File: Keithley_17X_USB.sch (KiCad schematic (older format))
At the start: 42 parts, among them J1 USB_B, J2 SIGNAL INPUT, J3 PROG, U1 TLP281-4, U2 TLP281-4, U3 MIC5504-3.3YM5, U4 MSP430FR2110, U5 FT230XS

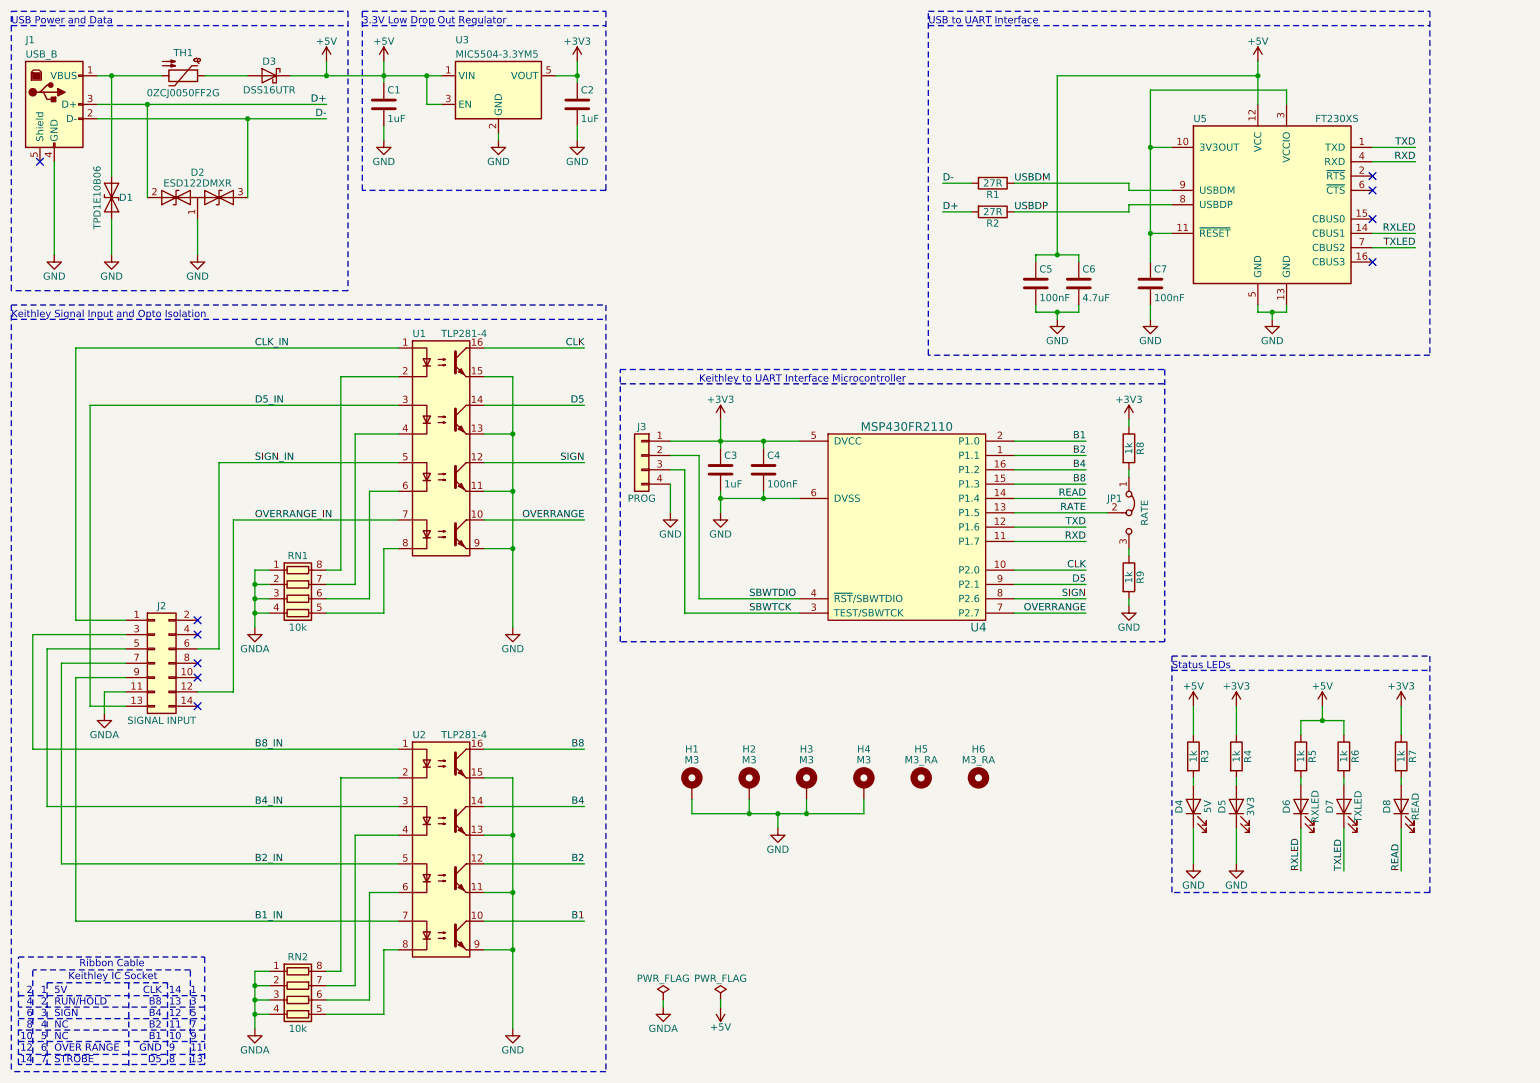
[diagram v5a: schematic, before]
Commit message: connect usb sheild to ground
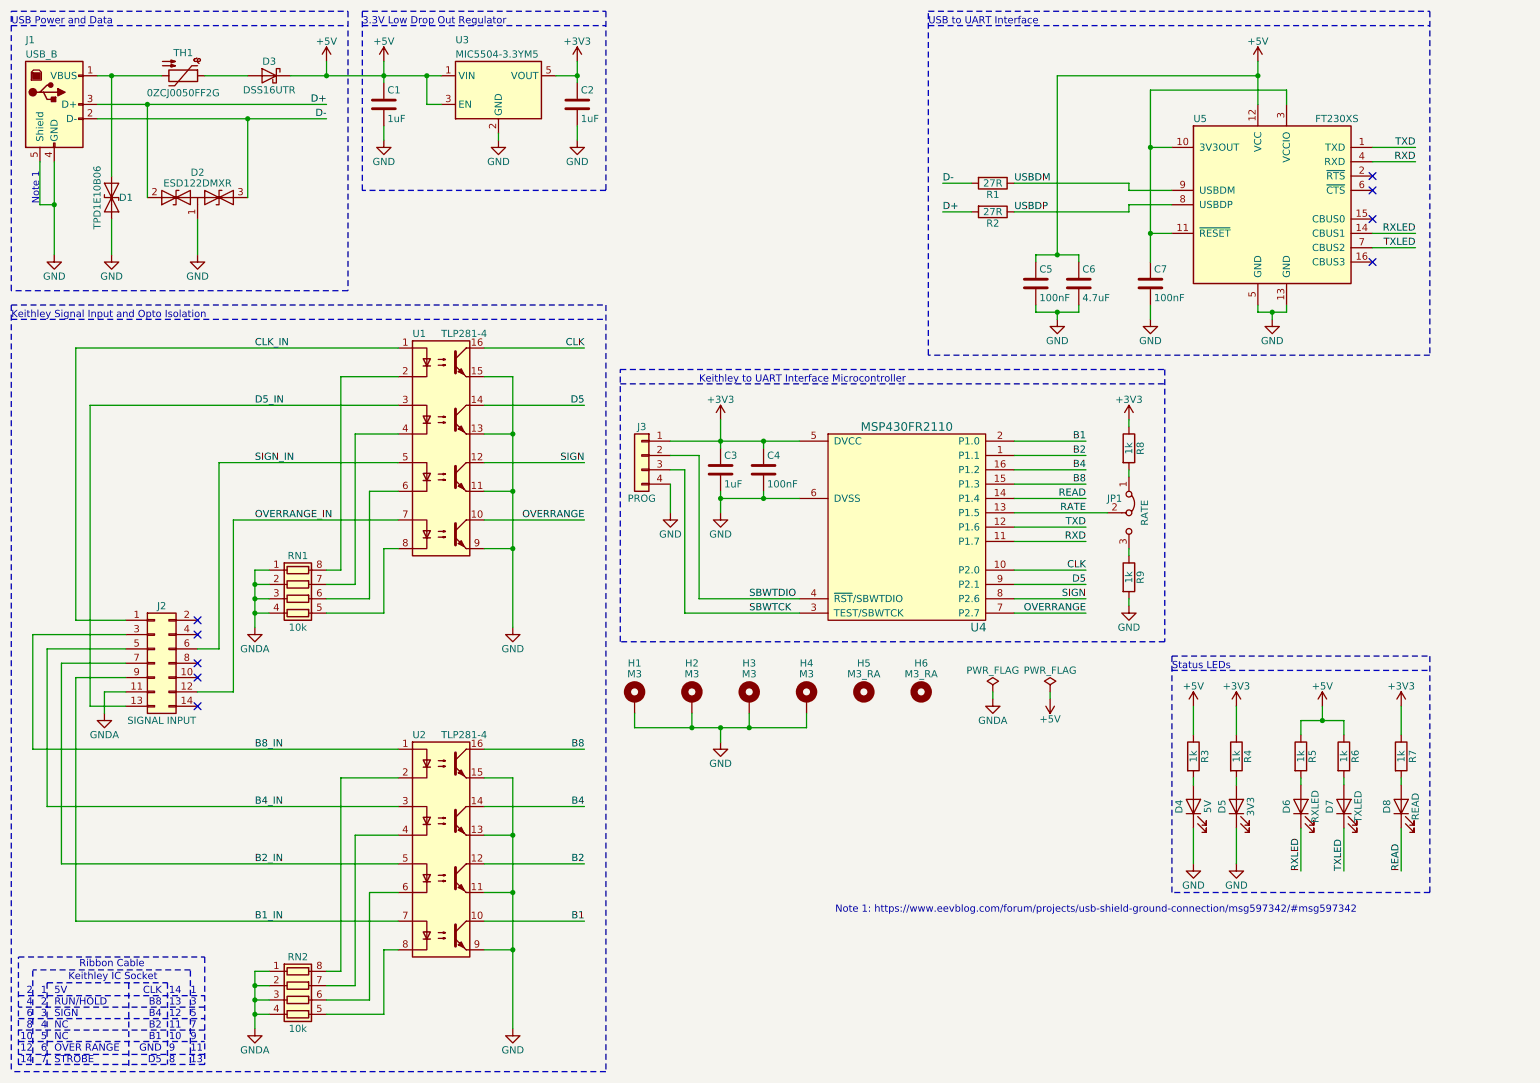
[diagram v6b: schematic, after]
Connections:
- net GND: now also J1.5 (Shield)
- no-connect marks 10 -> 9
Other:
- note added: "Note 1"
- note added: "Note 1: https://www.eevblog.com/forum/projects/usb-shield-ground-connection/msg597342/#msg597342"
- moved on the sheet: H1, H2, H3, H4, H5, H6
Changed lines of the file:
@@
 	1    0    0    -1
 $EndComp
-NoConn ~ 750  1600
 $Comp
 L power:GND #PWR026
@@
 $EndComp
 Wire Wire Line
-	850  1600 850  2250
+	850  1600 850  1900
 $Comp
 L power:GND #PWR03
@@
 L Mechanical:MountingHole_Pad H1
 U 1 1 5C68020E
-P 5300 5950
-F 0 "H1" H 5300 6200 50  0000 C CNN
-F 1 "M3" H 5300 6125 50  0000 C CNN
-F 2 "MountingHole:MountingHole_3.2mm_M3_DIN965_Pad" H 5300 5950 50  0001 C CNN
-F 3 "~" H 5300 5950 50  0001 C CNN
-	1    5300 5950
+P 4900 5350
+F 0 "H1" H 4900 5600 50  0000 C CNN
+F 1 "M3" H 4900 5525 50  0000 C CNN
+F 2 "MountingHole:MountingHole_3.2mm_M3_DIN965_Pad" H 4900 5350 50  0001 C CNN
+F 3 "~" H 4900 5350 50  0001 C CNN
+	1    4900 5350
 	1    0    0    -1
 $EndComp
@@
 L power:GND #PWR018
 U 1 1 5C680CDB
-P 5900 6250
-F 0 "#PWR018" H 5900 6000 50  0001 C CNN
-F 1 "GND" H 5900 6100 50  0000 C CNN
-F 2 "" H 5900 6250 50  0001 C CNN
-F 3 "" H 5900 6250 50  0001 C CNN
-	1    5900 6250
-	1    0    0    -1
-$EndComp
-Wire Wire Line
-	5300 6050 5300 6150
-Wire Wire Line
-	5300 6150 5700 6150
-Wire Wire Line
-	6500 6150 6500 6050
-Wire Wire Line
-	6100 6050 6100 6150
-Connection ~ 6100 6150
-Wire Wire Line
-	6100 6150 6500 6150
-Wire Wire Line
-	5700 6050 5700 6150
-Connection ~ 5700 6150
-Wire Wire Line
-	5700 6150 5900 6150
-Wire Wire Line
-	5900 6250 5900 6150
-Connection ~ 5900 6150
-Wire Wire Line
-	5900 6150 6100 6150
+P 5500 5650
+F 0 "#PWR018" H 5500 5400 50  0001 C CNN
+F 1 "GND" H 5500 5500 50  0000 C CNN
+F 2 "" H 5500 5650 50  0001 C CNN
+F 3 "" H 5500 5650 50  0001 C CNN
+	1    5500 5650
+	1    0    0    -1
+$EndComp
+Wire Wire Line
+	4900 5450 4900 5550
+Wire Wire Line
+	4900 5550 5300 5550
+Wire Wire Line
+	6100 5550 6100 5450
+Wire Wire Line
+	5700 5450 5700 5550
+Connection ~ 5700 5550
+Wire Wire Line
+	5700 5550 6100 5550
+Wire Wire Line
+	5300 5450 5300 5550
+Connection ~ 5300 5550
+Wire Wire Line
+	5300 5550 5500 5550
+Wire Wire Line
+	5500 5650 5500 5550
+Connection ~ 5500 5550
+Wire Wire Line
+	5500 5550 5700 5550
 $Comp
 L Mechanical:MountingHole_Pad H2
 U 1 1 5C6B7AB1
-P 5700 5950
-F 0 "H2" H 5700 6200 50  0000 C CNN
-F 1 "M3" H 5700 6125 50  0000 C CNN
-F 2 "MountingHole:MountingHole_3.2mm_M3_DIN965_Pad" H 5700 5950 50  0001 C CNN
-F 3 "~" H 5700 5950 50  0001 C CNN
-	1    5700 5950
+P 5300 5350
+F 0 "H2" H 5300 5600 50  0000 C CNN
+F 1 "M3" H 5300 5525 50  0000 C CNN
+F 2 "MountingHole:MountingHole_3.2mm_M3_DIN965_Pad" H 5300 5350 50  0001 C CNN
+F 3 "~" H 5300 5350 50  0001 C CNN
+	1    5300 5350
 	1    0    0    -1
 $EndComp
@@
 L Mechanical:MountingHole_Pad H3
 U 1 1 5C6B7B0F
-P 6100 5950
-F 0 "H3" H 6100 6200 50  0000 C CNN
-F 1 "M3" H 6100 6125 50  0000 C CNN
-F 2 "MountingHole:MountingHole_3.2mm_M3_DIN965_Pad" H 6100 5950 50  0001 C CNN
-F 3 "~" H 6100 5950 50  0001 C CNN
-	1    6100 5950
+P 5700 5350
+F 0 "H3" H 5700 5600 50  0000 C CNN
+F 1 "M3" H 5700 5525 50  0000 C CNN
+F 2 "MountingHole:MountingHole_3.2mm_M3_DIN965_Pad" H 5700 5350 50  0001 C CNN
+F 3 "~" H 5700 5350 50  0001 C CNN
+	1    5700 5350
 	1    0    0    -1
 $EndComp
@@
 L Mechanical:MountingHole_Pad H4
 U 1 1 5C6B7B6B
-P 6500 5950
-F 0 "H4" H 6500 6200 50  0000 C CNN
-F 1 "M3" H 6500 6125 50  0000 C CNN
-F 2 "MountingHole:MountingHole_3.2mm_M3_DIN965_Pad" H 6500 5950 50  0001 C CNN
-F 3 "~" H 6500 5950 50  0001 C CNN
-	1    6500 5950
+P 6100 5350
+F 0 "H4" H 6100 5600 50  0000 C CNN
+F 1 "M3" H 6100 5525 50  0000 C CNN
+F 2 "MountingHole:MountingHole_3.2mm_M3_DIN965_Pad" H 6100 5350 50  0001 C CNN
+F 3 "~" H 6100 5350 50  0001 C CNN
+	1    6100 5350
 	1    0    0    -1
 $EndComp
@@
 L power:PWR_FLAG #FLG0101
 U 1 1 5C804C0D
-P 5100 7450
-F 0 "#FLG0101" H 5100 7525 50  0001 C CNN
-F 1 "PWR_FLAG" H 5100 7600 50  0000 C CNN
-F 2 "" H 5100 7450 50  0001 C CNN
-F 3 "~" H 5100 7450 50  0001 C CNN
-	1    5100 7450
+P 7400 5300
+F 0 "#FLG0101" H 7400 5375 50  0001 C CNN
+F 1 "PWR_FLAG" H 7400 5450 50  0000 C CNN
+F 2 "" H 7400 5300 50  0001 C CNN
+F 3 "~" H 7400 5300 50  0001 C CNN
+	1    7400 5300
 	1    0    0    -1
 $EndComp
@@
 L power:GNDA #PWR0101
 U 1 1 5C804D47
-P 5100 7500
-F 0 "#PWR0101" H 5100 7250 50  0001 C CNN
-F 1 "GNDA" H 5100 7350 50  0000 C CNN
-F 2 "" H 5100 7500 50  0001 C CNN
-F 3 "" H 5100 7500 50  0001 C CNN
-	1    5100 7500
-	1    0    0    -1
-$EndComp
-Wire Wire Line
-	5100 7500 5100 7450
+P 7400 5350
+F 0 "#PWR0101" H 7400 5100 50  0001 C CNN
+F 1 "GNDA" H 7400 5200 50  0000 C CNN
+F 2 "" H 7400 5350 50  0001 C CNN
+F 3 "" H 7400 5350 50  0001 C CNN
+	1    7400 5350
+	1    0    0    -1
+$EndComp
+Wire Wire Line
+	7400 5350 7400 5300
 $Comp
 L power:+5V #PWR0102
 U 1 1 5C830718
-P 5500 7500
-F 0 "#PWR0102" H 5500 7350 50  0001 C CNN
-F 1 "+5V" H 5500 7640 50  0000 C CNN
-F 2 "" H 5500 7500 50  0001 C CNN
-F 3 "" H 5500 7500 50  0001 C CNN
-	1    5500 7500
+P 7800 5350
+F 0 "#PWR0102" H 7800 5200 50  0001 C CNN
+F 1 "+5V" H 7800 5490 50  0000 C CNN
+F 2 "" H 7800 5350 50  0001 C CNN
+F 3 "" H 7800 5350 50  0001 C CNN
+	1    7800 5350
 	-1   0    0    1
 $EndComp
@@
 L power:PWR_FLAG #FLG0102
 U 1 1 5C84C9A6
-P 5500 7450
-F 0 "#FLG0102" H 5500 7525 50  0001 C CNN
-F 1 "PWR_FLAG" H 5500 7600 50  0000 C CNN
-F 2 "" H 5500 7450 50  0001 C CNN
-F 3 "~" H 5500 7450 50  0001 C CNN
-	1    5500 7450
-	1    0    0    -1
-$EndComp
-Wire Wire Line
-	5500 7450 5500 7500
+P 7800 5300
+F 0 "#FLG0102" H 7800 5375 50  0001 C CNN
+F 1 "PWR_FLAG" H 7800 5450 50  0000 C CNN
+F 2 "" H 7800 5300 50  0001 C CNN
+F 3 "~" H 7800 5300 50  0001 C CNN
+	1    7800 5300
+	1    0    0    -1
+$EndComp
+Wire Wire Line
+	7800 5300 7800 5350
 $Comp
 L Mechanical:MountingHole H5
 U 1 1 5C6C1140
-P 6900 5900
-F 0 "H5" H 6900 6100 50  0000 C CNN
-F 1 "M3_RA" H 6900 6025 50  0000 C CNN
-F 2 "Terminal_Keystone:Keystone_Screw-Terminal_7761_RightAngle" H 6900 5900 50  0001 C CNN
-F 3 "http://www.keyelco.com/product-pdf.cfm?p=3928" H 6900 5900 50  0001 C CNN
-F 4 "TERM SCREW M3 4 PIN PCB RA" H 6900 5900 50  0001 C CNN "Description"
-F 5 "Keystone Electronics" H 6900 5900 50  0001 C CNN "Manufacture"
-F 6 "7761" H 6900 5900 50  0001 C CNN "Mfg Part Number"
-F 7 "Digi-Key" H 6900 5900 50  0001 C CNN "Supplier"
-F 8 "36-7761-ND" H 6900 5900 50  0001 C CNN "Supplier Part Number"
-	1    6900 5900
+P 6500 5300
+F 0 "H5" H 6500 5500 50  0000 C CNN
+F 1 "M3_RA" H 6500 5425 50  0000 C CNN
+F 2 "Terminal_Keystone:Keystone_Screw-Terminal_7761_RightAngle" H 6500 5300 50  0001 C CNN
+F 3 "http://www.keyelco.com/product-pdf.cfm?p=3928" H 6500 5300 50  0001 C CNN
+F 4 "TERM SCREW M3 4 PIN PCB RA" H 6500 5300 50  0001 C CNN "Description"
+F 5 "Keystone Electronics" H 6500 5300 50  0001 C CNN "Manufacture"
+F 6 "7761" H 6500 5300 50  0001 C CNN "Mfg Part Number"
+F 7 "Digi-Key" H 6500 5300 50  0001 C CNN "Supplier"
+F 8 "36-7761-ND" H 6500 5300 50  0001 C CNN "Supplier Part Number"
+	1    6500 5300
 	1    0    0    -1
 $EndComp
@@
 L Mechanical:MountingHole H6
 U 1 1 5C6C2A25
-P 7300 5900
-F 0 "H6" H 7300 6100 50  0000 C CNN
-F 1 "M3_RA" H 7300 6025 50  0000 C CNN
-F 2 "Terminal_Keystone:Keystone_Screw-Terminal_7761_RightAngle" H 7300 5900 50  0001 C CNN
-F 3 "http://www.keyelco.com/product-pdf.cfm?p=3928" H 7300 5900 50  0001 C CNN
-F 4 "TERM SCREW M3 4 PIN PCB RA" H 7300 5900 50  0001 C CNN "Description"
-F 5 "Keystone Electronics" H 7300 5900 50  0001 C CNN "Manufacture"
-F 6 "7761" H 7300 5900 50  0001 C CNN "Mfg Part Number"
-F 7 "Digi-Key" H 7300 5900 50  0001 C CNN "Supplier"
-F 8 "36-7761-ND" H 7300 5900 50  0001 C CNN "Supplier Part Number"
-	1    7300 5900
+P 6900 5300
+F 0 "H6" H 6900 5500 50  0000 C CNN
+F 1 "M3_RA" H 6900 5425 50  0000 C CNN
+F 2 "Terminal_Keystone:Keystone_Screw-Terminal_7761_RightAngle" H 6900 5300 50  0001 C CNN
+F 3 "http://www.keyelco.com/product-pdf.cfm?p=3928" H 6900 5300 50  0001 C CNN
+F 4 "TERM SCREW M3 4 PIN PCB RA" H 6900 5300 50  0001 C CNN "Description"
+F 5 "Keystone Electronics" H 6900 5300 50  0001 C CNN "Manufacture"
+F 6 "7761" H 6900 5300 50  0001 C CNN "Mfg Part Number"
+F 7 "Digi-Key" H 6900 5300 50  0001 C CNN "Supplier"
+F 8 "36-7761-ND" H 6900 5300 50  0001 C CNN "Supplier Part Number"
+	1    6900 5300
 	1    0    0    -1
 $EndComp
@@
 Text Label 7550 1950 0    50   ~ 0
 USBDP
+Wire Wire Line
+	750  1600 750  1900
+Wire Wire Line
+	750  1900 850  1900
+Connection ~ 850  1900
+Wire Wire Line
+	850  1900 850  2250
+Text Notes 750  1900 1    50   ~ 0
+Note 1
+Text Notes 6300 6850 0    50   ~ 0
+Note 1: https://www.eevblog.com/forum/projects/usb-shield-ground-connection/msg597342/#msg597342
 $EndSCHEMATC

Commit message: ground right angle mounts
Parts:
- H5, H6: symbol Mechanical:MountingHole -> Mechanical:MountingHole_Pad
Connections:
- net GND: now also H5.1, H6.1
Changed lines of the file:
@@
 	7800 5300 7800 5350
 $Comp
-L Mechanical:MountingHole H5
+L Mechanical:MountingHole_Pad H5
 U 1 1 5C6C1140
-P 6500 5300
-F 0 "H5" H 6500 5500 50  0000 C CNN
-F 1 "M3_RA" H 6500 5425 50  0000 C CNN
-F 2 "Terminal_Keystone:Keystone_Screw-Terminal_7761_RightAngle" H 6500 5300 50  0001 C CNN
-F 3 "http://www.keyelco.com/product-pdf.cfm?p=3928" H 6500 5300 50  0001 C CNN
-F 4 "TERM SCREW M3 4 PIN PCB RA" H 6500 5300 50  0001 C CNN "Description"
-F 5 "Keystone Electronics" H 6500 5300 50  0001 C CNN "Manufacture"
-F 6 "7761" H 6500 5300 50  0001 C CNN "Mfg Part Number"
-F 7 "Digi-Key" H 6500 5300 50  0001 C CNN "Supplier"
-F 8 "36-7761-ND" H 6500 5300 50  0001 C CNN "Supplier Part Number"
-	1    6500 5300
+P 6550 5350
+F 0 "H5" H 6550 5550 50  0000 C CNN
+F 1 "M3_RA" H 6550 5475 50  0000 C CNN
+F 2 "Terminal_Keystone:Keystone_Screw-Terminal_7761_RightAngle" H 6550 5350 50  0001 C CNN
+F 3 "http://www.keyelco.com/product-pdf.cfm?p=3928" H 6550 5350 50  0001 C CNN
+F 4 "TERM SCREW M3 4 PIN PCB RA" H 6550 5350 50  0001 C CNN "Description"
+F 5 "Keystone Electronics" H 6550 5350 50  0001 C CNN "Manufacture"
+F 6 "7761" H 6550 5350 50  0001 C CNN "Mfg Part Number"
+F 7 "Digi-Key" H 6550 5350 50  0001 C CNN "Supplier"
+F 8 "36-7761-ND" H 6550 5350 50  0001 C CNN "Supplier Part Number"
+	1    6550 5350
 	1    0    0    -1
 $EndComp
 $Comp
-L Mechanical:MountingHole H6
+L Mechanical:MountingHole_Pad H6
 U 1 1 5C6C2A25
-P 6900 5300
-F 0 "H6" H 6900 5500 50  0000 C CNN
-F 1 "M3_RA" H 6900 5425 50  0000 C CNN
-F 2 "Terminal_Keystone:Keystone_Screw-Terminal_7761_RightAngle" H 6900 5300 50  0001 C CNN
-F 3 "http://www.keyelco.com/product-pdf.cfm?p=3928" H 6900 5300 50  0001 C CNN
-F 4 "TERM SCREW M3 4 PIN PCB RA" H 6900 5300 50  0001 C CNN "Description"
-F 5 "Keystone Electronics" H 6900 5300 50  0001 C CNN "Manufacture"
-F 6 "7761" H 6900 5300 50  0001 C CNN "Mfg Part Number"
-F 7 "Digi-Key" H 6900 5300 50  0001 C CNN "Supplier"
-F 8 "36-7761-ND" H 6900 5300 50  0001 C CNN "Supplier Part Number"
-	1    6900 5300
+P 6900 5350
+F 0 "H6" H 6900 5550 50  0000 C CNN
+F 1 "M3_RA" H 6900 5475 50  0000 C CNN
+F 2 "Terminal_Keystone:Keystone_Screw-Terminal_7761_RightAngle" H 6900 5350 50  0001 C CNN
+F 3 "http://www.keyelco.com/product-pdf.cfm?p=3928" H 6900 5350 50  0001 C CNN
+F 4 "TERM SCREW M3 4 PIN PCB RA" H 6900 5350 50  0001 C CNN "Description"
+F 5 "Keystone Electronics" H 6900 5350 50  0001 C CNN "Manufacture"
+F 6 "7761" H 6900 5350 50  0001 C CNN "Mfg Part Number"
+F 7 "Digi-Key" H 6900 5350 50  0001 C CNN "Supplier"
+F 8 "36-7761-ND" H 6900 5350 50  0001 C CNN "Supplier Part Number"
+	1    6900 5350
 	1    0    0    -1
 $EndComp
@@
 Text Notes 6300 6850 0    50   ~ 0
 Note 1: https://www.eevblog.com/forum/projects/usb-shield-ground-connection/msg597342/#msg597342
+Wire Wire Line
+	6550 5450 6550 5650
+Wire Wire Line
+	6900 5450 6900 5650
+$Comp
+L power:GND #PWR?
+U 1 1 5C93C3FD
+P 6550 5650
+F 0 "#PWR?" H 6550 5400 50  0001 C CNN
+F 1 "GND" H 6550 5500 50  0000 C CNN
+F 2 "" H 6550 5650 50  0001 C CNN
+F 3 "" H 6550 5650 50  0001 C CNN
+	1    6550 5650
+	1    0    0    -1
+$EndComp
+$Comp
+L power:GND #PWR?
+U 1 1 5C93C45C
+P 6900 5650
+F 0 "#PWR?" H 6900 5400 50  0001 C CNN
+F 1 "GND" H 6900 5500 50  0000 C CNN
+F 2 "" H 6900 5650 50  0001 C CNN
+F 3 "" H 6900 5650 50  0001 C CNN
+	1    6900 5650
+	1    0    0    -1
+$EndComp
 $EndSCHEMATC

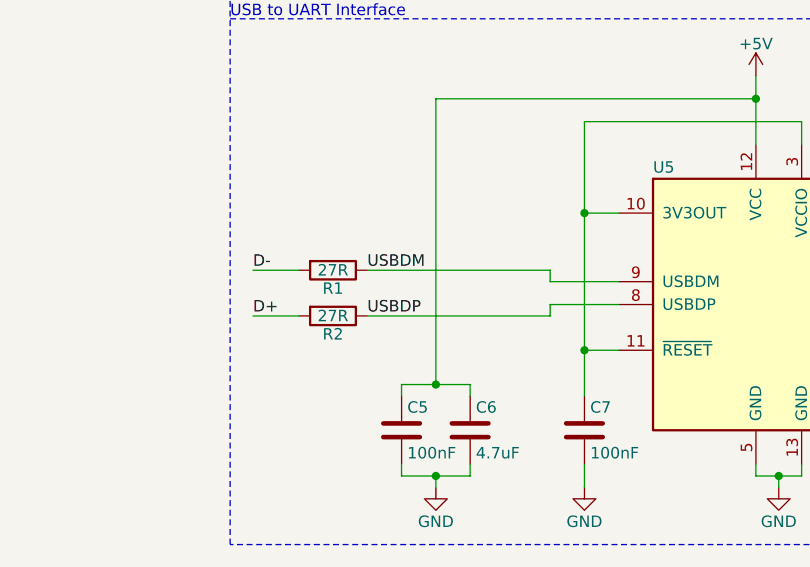
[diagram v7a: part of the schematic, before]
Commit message: rename usb differential pairs to what kicad expects
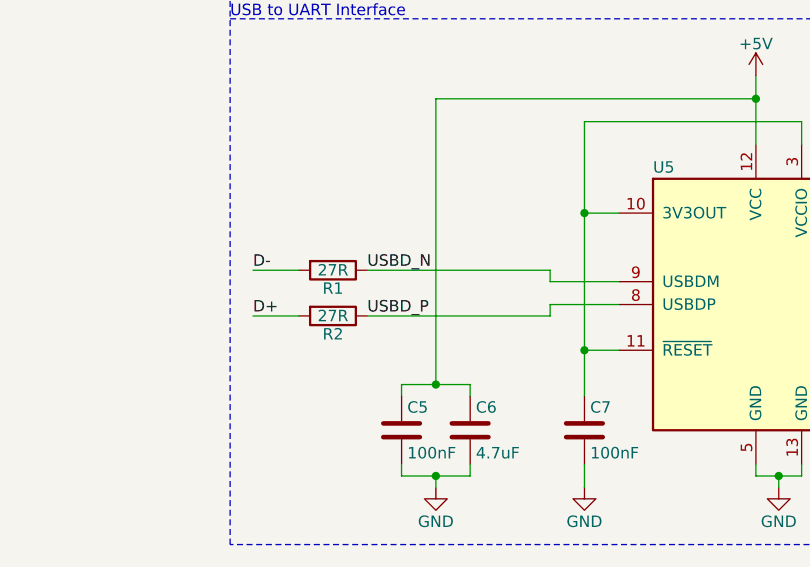
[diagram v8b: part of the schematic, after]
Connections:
- net USBDM renamed USBD_N
- net USBDP renamed USBD_P
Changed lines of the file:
@@
 RATE
 Text Label 7550 1750 0    50   ~ 0
-USBDM
+USBD_N
 Text Label 7550 1950 0    50   ~ 0
-USBDP
+USBD_P
 Wire Wire Line
 	750  1600 750  1900
@@
 	6900 5450 6900 5650
 $Comp
-L power:GND #PWR?
+L power:GND #PWR0105
 U 1 1 5C93C3FD
 P 6550 5650
-F 0 "#PWR?" H 6550 5400 50  0001 C CNN
+F 0 "#PWR0105" H 6550 5400 50  0001 C CNN
 F 1 "GND" H 6550 5500 50  0000 C CNN
 F 2 "" H 6550 5650 50  0001 C CNN
@@
 $EndComp
 $Comp
-L power:GND #PWR?
+L power:GND #PWR0106
 U 1 1 5C93C45C
 P 6900 5650
-F 0 "#PWR?" H 6900 5400 50  0001 C CNN
+F 0 "#PWR0106" H 6900 5400 50  0001 C CNN
 F 1 "GND" H 6900 5500 50  0000 C CNN
 F 2 "" H 6900 5650 50  0001 C CNN
